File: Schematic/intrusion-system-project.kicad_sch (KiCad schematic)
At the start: 18 parts

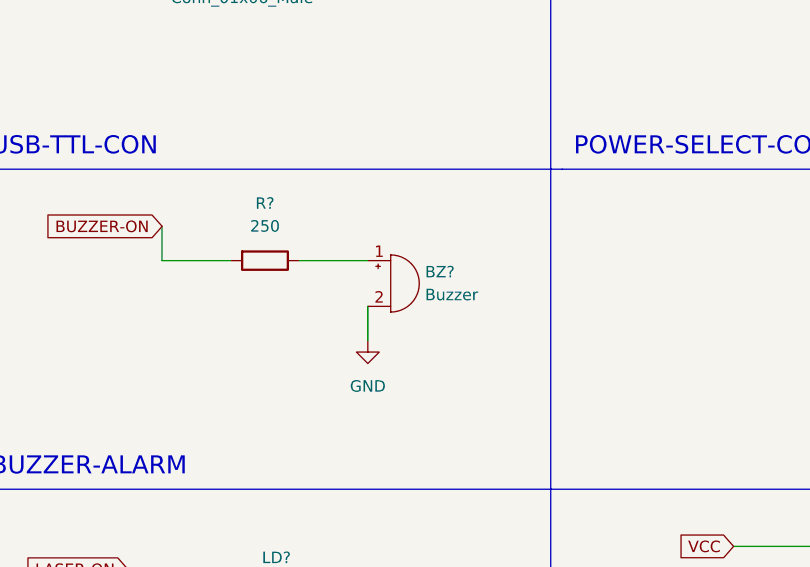
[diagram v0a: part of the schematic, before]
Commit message: Refactor file structure
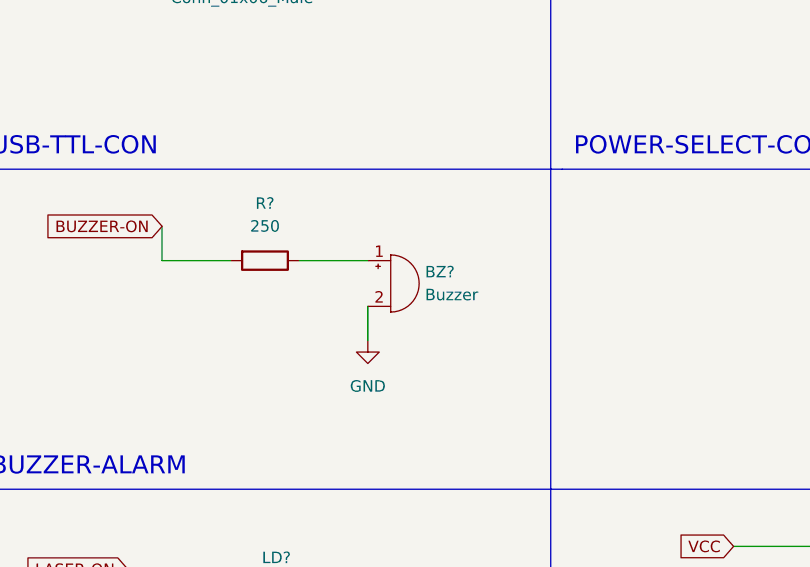
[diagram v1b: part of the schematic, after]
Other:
- title: (none) -> Laser-security-system
